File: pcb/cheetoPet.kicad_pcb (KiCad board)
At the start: 2 copper layers, 38 x 61 mm, 94 parts, among them CN1 bat connector, J2 USB_C_Receptacle_USB2.0_16P, Q1 FS8205A, Q2 BSS138, SW1 POWER, SW10 RESET, SW7 B, SW8 A, SW9 X, U1 USBLC6-2SC6, U10 TPS63802DLAR, U11 KLJ-01304T-08R07W, U2 MAX98357A, U3 DW01A, U4 BQ24074RGT, U5 MAX17048G_T10, U6 LSM6DSL, U7 RV-3028-C7, U8 ESP32-S3-MINI-1U, U9 WS-003DB

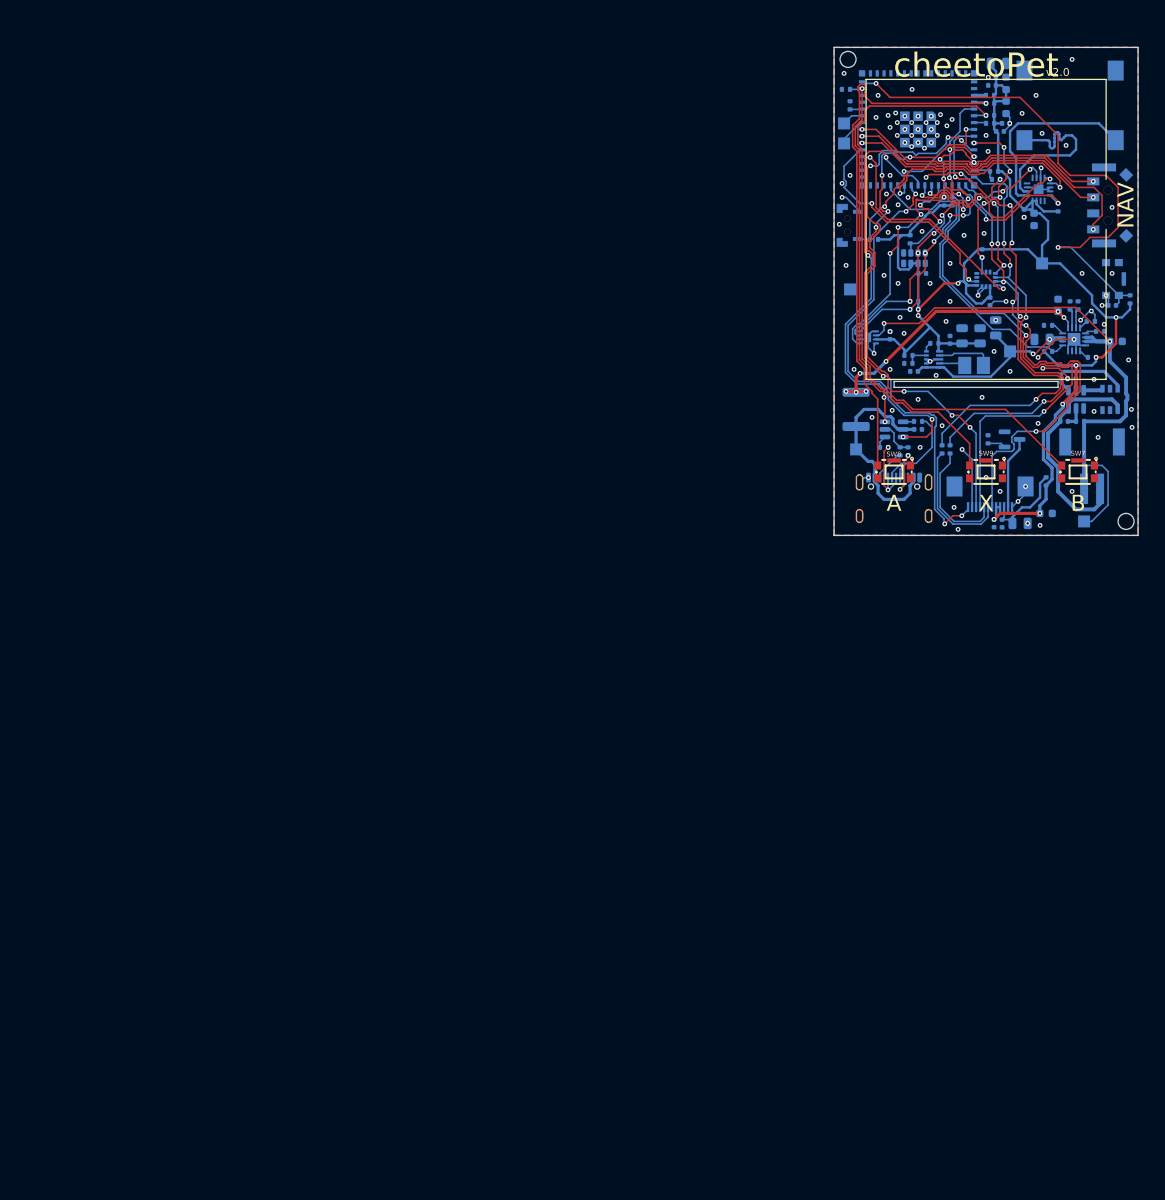
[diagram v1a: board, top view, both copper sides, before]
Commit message: pcb v2.1 schematic finished
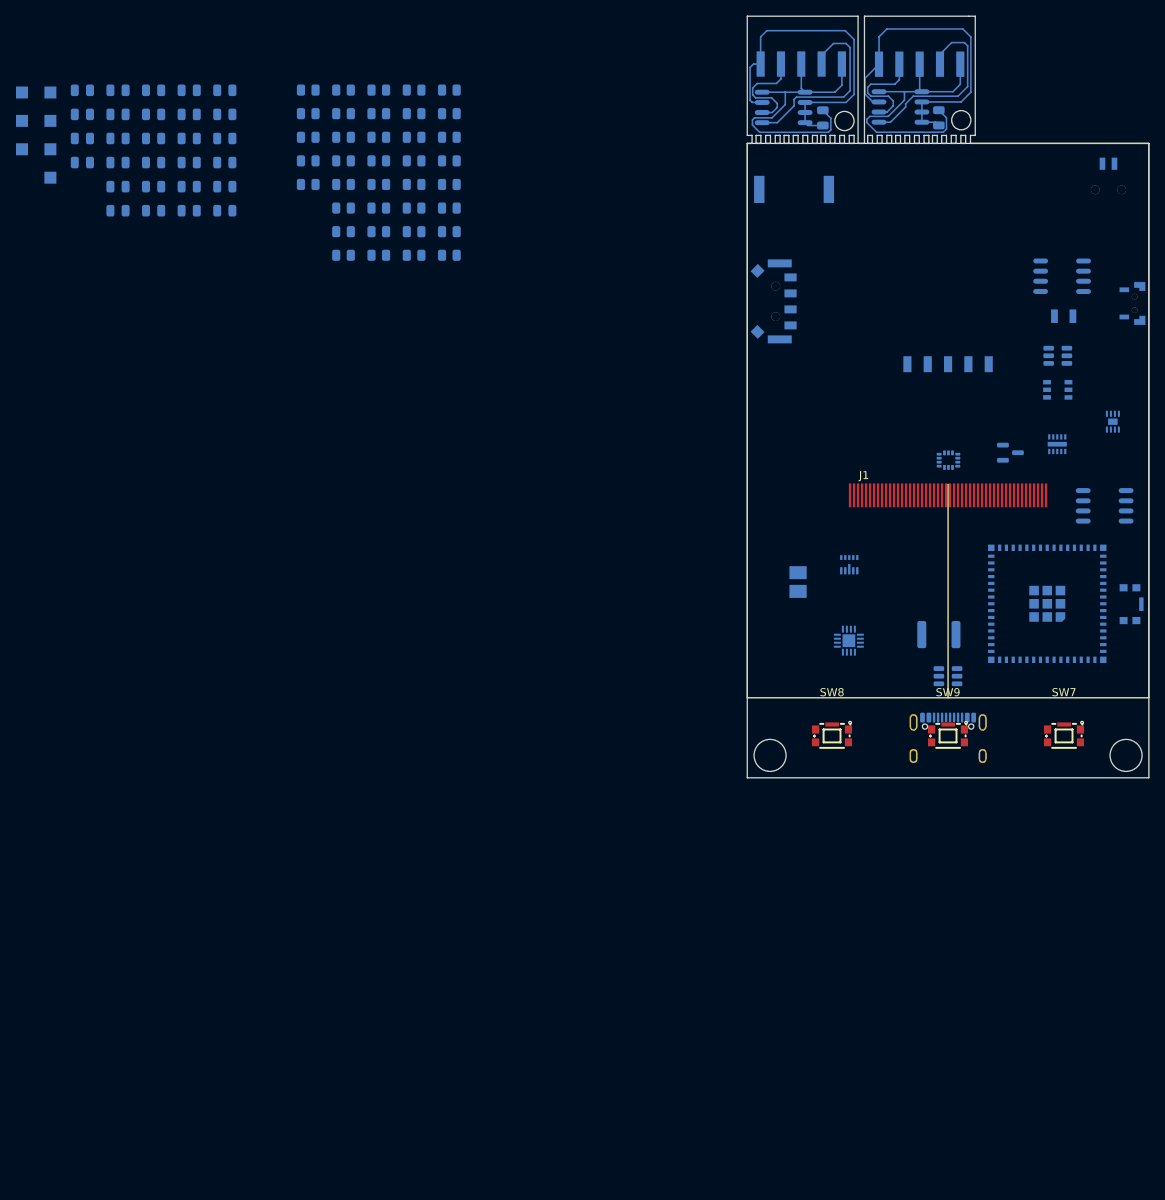
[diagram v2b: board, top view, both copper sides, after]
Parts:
- removed C11: 100nF, Capacitor_SMD:C_0402_1005Metric
- removed C12: 10uF, Capacitor_SMD:C_0603_1608Metric
- removed CN1: bat connector, EasyEDA:CONN-SMD_P2.00_S2B-PH-SM4-TB-LF-SN
- removed FPC1: FPC-05F-12PH20, EasyEDA:FPC-SMD_12P-P0.50_FPC-05F-12PH20
- removed R13: 10k, Resistor_SMD:R_0402_1005Metric
- removed R6: 0, Resistor_SMD:R_0402_1005Metric
- added BUZZER1: CPT-9019A-SMT-TR, EasyEDA:BUZ-SMD_L9.0-W9.0_CPT-9019A-SMT-TR, B.Cu at (128.5, 63.8)
- added C29: 100nF, Capacitor_SMD:C_0805_2012Metric, B.Cu at (39.5, 54.4)
- added C30: 1uF, Capacitor_SMD:C_0805_2012Metric, B.Cu at (39.5, 57.4)
- added C31: 100nF, Capacitor_SMD:C_0805_2012Metric, B.Cu at (39.5, 60.4)
- added C32: 100nF, Capacitor_SMD:C_0805_2012Metric, B.Cu at (132.1, 54.8)
- added C33: 100nF, Capacitor_SMD:C_0805_2012Metric, B.Cu at (146.6, 54.8)
- added CN2: S2B-ZR-SM2-TF, EasyEDA:CONN-SMD_2P-P1.50_S2B-ZR-SM2-TF-LF-SN, B.Cu at (167.8, 60.5)
- added H1: HX PZ2.54-1X5P WT, EasyEDA:HDR-SMD_5P-P2.54-H-M-W12.8-N, B.Cu at (129.4, 48.1)
- added H2: HX PZ2.54-1X5P WT, EasyEDA:HDR-SMD_5P-P2.54-H-M-W12.8-N, B.Cu at (144.2, 48.1)
- added J1: ER-TFT028A3-4, footprints:FPC-50pin,0.5Pitch, F.Cu at (148.0, 102.0)
- added R39: 22, Resistor_SMD:R_0805_2012Metric, B.Cu at (67.8, 60.2)
- added R40: 22, Resistor_SMD:R_0805_2012Metric, B.Cu at (67.8, 63.1)
- added U12: LTC2955CDDB-1#TRPBF, EasyEDA:DFN-10_L3.0-W2.0-P0.50-BL-EP, B.Cu at (161.4, 95.6)
- added U13: AT24C32M/TR, EasyEDA:SOP-8_L4.9-W3.9-P1.27-LS6.0-BL, B.Cu at (127.2, 53.5)
- added U14: AT24C32M/TR, EasyEDA:SOP-8_L4.9-W3.9-P1.27-LS6.0-BL, B.Cu at (141.8, 53.5)
- added X1: SC-32S32.768kHz20PPM7pF, EasyEDA:OSC-SMD_L3.2-W1.5, B.Cu at (162.2, 79.6)
- C1, C15, C16, C18, C21, C24, C25, C4, C5, C6, C7: footprint Capacitor_SMD:C_0402_1005Metric -> Capacitor_SMD:C_0805_2012Metric
- C17, C19, C26: value 0.1uF -> 100nF; footprint Capacitor_SMD:C_0402_1005Metric -> Capacitor_SMD:C_0805_2012Metric
- C2, C20, C3: footprint Capacitor_SMD:C_0603_1608Metric -> Capacitor_SMD:C_0805_2012Metric
- C8, C9: value 10uF X5R -> 10uF; footprint Capacitor_SMD:C_0603_1608Metric -> Capacitor_SMD:C_0805_2012Metric
- R1, R10, R11, R12, R15, R16, R17, R18, R19, R2, R20, R21, R22, R23, R24, R25, R26, R27, R28, R29, R3, R30, R31, R32, R33, R34, R35, R36, R37, R38, R4, R5, R7, R8, R9: footprint Resistor_SMD:R_0402_1005Metric -> Resistor_SMD:R_0805_2012Metric
- SW1: value POWER -> TS24CA; footprint EasyEDA:SW-SMD_LXTD-0204-034 -> EasyEDA:SW-SMD_2P-TS24CA
- U11: value KLJ-01304T-08R07W -> AT24C32M/TR; footprint EasyEDA:BUZ-SMD_4P-L13.0-W13.0-P11.4-BL -> EasyEDA:SOP-8_L4.9-W3.9-P1.27-LS6.0-BL
- U2: value MAX98357A -> HX PM2.54-1X5P WT; footprint Package_DFN_QFN:TQFN-16-1EP_3x3mm_P0.5mm_EP1.23x1.23mm -> EasyEDA:HDR-SMD_5P-P2.54-H-F
- U7: value RV-3028-C7 -> PCF8523T/1,118; footprint Package_SON:MicroCrystal_C7_SON-8_1.5x3.2mm_P0.9mm -> EasyEDA:SOP-8_L4.9-W3.9-P1.27-LS6.0-BL
- moved TP2 138.6 mm to (35.5, 55.2)
- moved C28 129.1 mm to (39.5, 51.4), turned to 180 degrees
- moved C25 125.6 mm to (44.0, 60.4)
- moved TP4 124.4 mm to (35.5, 62.3)
- moved TP3 122.6 mm to (35.5, 58.7)
- moved C8 119.3 mm to (52.9, 54.4)
- moved C20 118.8 mm to (48.4, 63.4), turned to 180 degrees
- moved C26 118.3 mm to (44.0, 63.4), turned to 180 degrees
- moved C7 116.9 mm to (52.9, 51.4)
- moved C19 114.3 mm to (48.4, 60.4), turned to 180 degrees
- moved C27 111.6 mm to (44.0, 66.4)
- moved C23 111.3 mm to (44.0, 54.4), turned to 180 degrees
- moved C9 110.6 mm to (52.9, 57.4), turned to 180 degrees
- moved TP1 110.1 mm to (35.5, 51.6)
- moved C22 109.9 mm to (44.0, 51.4), turned to 180 degrees
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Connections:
- net Net-(U8-RXD0) renamed RX
- net Net-(U8-TXD0) renamed TX
- R26 pad 1: +3V3 -> CART_PRSNC
- R26 pad 2: POWER -> GND
- R29 pad 2: SPI_MOSI -> TFT_CS
- R30 pad 2: TFT_CS -> SPI_MOSI
- SW1 pad 1: POWER -> Net-(U12-~{PB})
- SW9 pad 3: GND -> +3V3
- U10 pad 1: OUT -> LATCH_EN
- U11 pad 1: SPKR+ -> GND
- U11 pad 2: SPKR- -> GND
- U11 pad 3: unconnected-(U11-DUMMY-Pad3) -> GND
- U11 pad 4: unconnected-(U11-DUMMY-Pad4) -> GND
- U2 pad 1: DAC_DIN -> GND
- U2 pad 2: GND -> SCL
- U2 pad 3: GND -> +3V3
- U2 pad 4: DAC_SD -> SDA
- U2 pad 5: unconnected-(U2-NC-Pad5) -> CART_PRSNC
- U6 pad 4: MPU_INT1 -> unconnected-(U6-INT1-Pad4)
- U6 pad 9: MPU_INT2 -> unconnected-(U6-INT2-Pad9)
- U7 pad 1: unconnected-(U7-CLKOUT-Pad1) -> Net-(U7-OSCI)
- U7 pad 2: RTC_INT -> Net-(U7-OSCO)
- U7 pad 3: SCL -> BAT+
- U7 pad 4: SDA -> GND
- U7 pad 5: GND -> SDA
- U7 pad 6: +3V3 -> SCL
- U7 pad 7: +3V3 -> RTC_INT
- U7 pad 8: unconnected-(U7-EVI-Pad8) -> +3V3
- U8 pad 17: DAC_SD -> TFT_PWM
- U8 pad 21: DAC_BCLK -> SPKR+
- U8 pad 22: DAC_LRCLK -> LATCH_KILL
- U8 pad 25: DAC_DIN -> CART_PRSNC
- U8 pad 3: Net-(U8-3V3) -> +3V3
- U8 pad 5: POWER -> LATCH_INT
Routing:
- net +3V3: track 176.8 -> 0.00 mm, vias 9 -> 0
- net B: track 80.3 -> 0.00 mm, vias 1 -> 0
- net BAT+: track 74.1 -> 0.00 mm, vias 2 -> 0
- net TFT_TE: track 73.8 -> 0.00 mm, vias 8 -> 0
- net TFT_DC: track 70.6 -> 0.00 mm, vias 6 -> 0
- net A: track 69.1 -> 0.00 mm, vias 1 -> 0
- net GND: track 68.6 -> 0.00 mm, vias 110 -> 0
- net EN: track 65.9 -> 0.00 mm, vias 2 -> 0
- net TFT_RES: track 62.9 -> 0.00 mm, vias 2 -> 0
- net Net-(J1-Pin_34): track 60.1 -> 0.00 mm, vias 6 -> 0
- net X: track 57.7 -> 0.00 mm, vias 1 -> 0
- net SPI_MOSI: track 54.9 -> 0.00 mm, vias 4 -> 0
- net SPI_SCL: track 52.8 -> 0.00 mm, vias 4 -> 0
- net PUSB_D-: track 47.8 -> 0.00 mm, vias 4 -> 0
- net PUSB_D+: track 46.6 -> 0.00 mm, vias 4 -> 0
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- removed copper zone on B.Cu, net GND
- removed copper zone on F.Cu, net GND
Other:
- board size 38 x 61 mm -> 50.2 x 95.2 mm
- board text removed: "A"
- board text removed: "B"
- board text removed: "CPU"
- board text removed: "EN"
- board text removed: "IMU"
- board text removed: "NAV"
- board text removed: "X"
- board text removed: "cheetoPet"
- board text removed: "designed by olly jeffery"
- board text removed: "v2.0"

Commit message: pcb tweaks
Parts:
- removed SW10: RESET, EasyEDA:SW-SMD_5P-L4.2-W2.8-P1.60-LS4.6-TR
- removed SW7: B, EasyEDA:SW-SMD_5P-L4.2-W2.8-P1.60-LS4.6-TR
- removed SW8: A, EasyEDA:SW-SMD_5P-L4.2-W2.8-P1.60-LS4.6-TR
- removed SW9: X, EasyEDA:SW-SMD_5P-L4.2-W2.8-P1.60-LS4.6-TR
- added SW1: BTN, EasyEDA:KEY-SMD_4P-L4.2-W2.8-P1.60-LS4.6, B.Cu at (128.9, 164.9)
- added SW2: BTN, EasyEDA:KEY-SMD_4P-L4.2-W2.8-P1.60-LS4.6, F.Cu at (91.7, 181.8)
- added SW3: BTN, EasyEDA:KEY-SMD_4P-L4.2-W2.8-P1.60-LS4.6, F.Cu at (120.8, 181.8)
- added SW4: BTN, EasyEDA:KEY-SMD_4P-L4.2-W2.8-P1.60-LS4.6, F.Cu at (106.2, 182.5)
- C1, C10, C14, C15, C16, C17, C18, C19, C2, C20, C21, C22, C23, C24, C25, C26, C27, C28, C29, C3, C30, C31, C32, C33, C4, C5, C6, C7, C8, C9: footprint Capacitor_SMD:C_0805_2012Metric -> customs:C_0805_2012Metric - CUSTOM TEXT
- R1, R10, R11, R12, R15, R16, R17, R18, R19, R2, R20, R21, R22, R23, R24, R25, R26, R27, R28, R29, R3, R30, R31, R32, R33, R34, R35, R36, R37, R38, R39, R4, R40, R5, R7, R8, R9: footprint Resistor_SMD:R_0805_2012Metric -> customs:R_0805_2012Metric - CUSTOM TEXT
- moved C2 141.3 mm to (127.7, 176.9), turned to -90 degrees
- moved C1 140.8 mm to (129.7, 172.1), turned to 90 degrees
- moved C3 138.8 mm to (124.8, 178.7), turned to 0 degrees
- moved C25 138.0 mm to (129.0, 169.1)
- moved C27 135.0 mm to (124.8, 174.5)
- moved C4 133.4 mm to (121.8, 177.2), turned to -90 degrees
- moved C5 131.8 mm to (124.8, 176.6), turned to 0 degrees
- moved C6 128.1 mm to (127.7, 173.4), turned to 90 degrees
- moved C22 126.4 mm to (103.0, 163.2), turned to 0 degrees
- moved R23 126.1 mm to (115.6, 180.1), turned to 90 degrees
- moved C29 125.2 mm to (121.9, 148.7)
- moved C8 125.2 mm to (98.0, 171.2), turned to 90 degrees
- moved R15 123.9 mm to (99.1, 182.7), turned to -90 degrees
- moved C31 123.4 mm to (125.7, 148.7), turned to 0 degrees
- moved C28 122.0 mm to (117.1, 145.6), turned to 90 degrees
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- renumbered SW1 to SW5
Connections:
- C32 pad 2: Net-(U13-A1) -> GND
- C33 pad 2: Net-(U14-A1) -> GND
- H1 pad 1: Net-(U13-A1) -> GND
- H2 pad 1: Net-(U14-A1) -> GND
- U13 pad 2: Net-(U13-A1) -> GND
- U13 pad 3: Net-(U13-A1) -> GND
- U13 pad 4: Net-(U13-A1) -> GND
- U13 pad 7: Net-(U13-A1) -> GND
- U14 pad 2: Net-(U14-A1) -> GND
- U14 pad 3: Net-(U14-A1) -> GND
- U14 pad 4: Net-(U14-A1) -> GND
- U14 pad 7: Net-(U14-A1) -> GND
- U6 pad 4: unconnected-(U6-INT1-Pad4) -> MPU_INT1
- U6 pad 9: unconnected-(U6-INT2-Pad9) -> MPU_INT2
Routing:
- net +3V3: track 0.00 -> 287.5 mm, vias 0 -> 5
- net GND: track 0.00 -> 205.1 mm, vias 0 -> 85
- net BAT+: track 0.00 -> 155.8 mm, vias 0 -> 5
- net SCL: track 0.00 -> 112.3 mm, vias 0 -> 6
- net SPKR+: track 0.00 -> 105.5 mm, vias 0 -> 2
- net SDA: track 0.00 -> 102.8 mm, vias 0 -> 7
- net TFT_CS: track 0.00 -> 80.5 mm, vias 0 -> 4
- net SPI_MOSI: track 0.00 -> 77.2 mm, vias 0 -> 5
- net RTC_INT: track 0.00 -> 75.9 mm, vias 0 -> 2
- net +5V: track 0.00 -> 74.7 mm, vias 0 -> 5
- net SPI_SCL: track 0.00 -> 72.4 mm, vias 0 -> 3
- net TX: track 0.00 -> 67.6 mm, vias 0 -> 2
- net RX: track 0.00 -> 67.2 mm, vias 0 -> 2
- net X: track 0.00 -> 64.3 mm, vias 0 -> 2
- net MPU_CS: track 0.00 -> 59.1 mm, vias 0 -> 6
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- added copper zone on B.Cu, net GND
- added copper zone on F.Cu, net GND
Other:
- outline, holes or cut-outs redrawn
- board text added: "3V3 | 5V"
- board text added: "BAT+ | TX"
- board text added: "ER-TFT028A3-4"
- board text added: "GND"
- board text added: "L"
- board text added: "OUT | RX"
- board text added: "R"
- board text added: "cheetoPet"
- board text added: "designed by olly jeffery"
- board text added: "pet name here..."
- board text added: "petCart"
- board text added: "petCart area"
- board text added: "v2.1"

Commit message: recon mpu
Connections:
- C16 pad 2: +3V3 -> BAT+
- U6 pad 5: +3V3 -> BAT+
- U6 pad 8: +3V3 -> BAT+
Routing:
- net BAT+: track 155.8 -> 181.5 mm, vias 5 -> 6
- net MPU_INT2: track 29.4 -> 28.2 mm
